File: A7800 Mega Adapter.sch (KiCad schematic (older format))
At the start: 8 parts, among them J1 Atari 7800, J2 Mega Drive, Q1 2N3906, Q2 2N3906

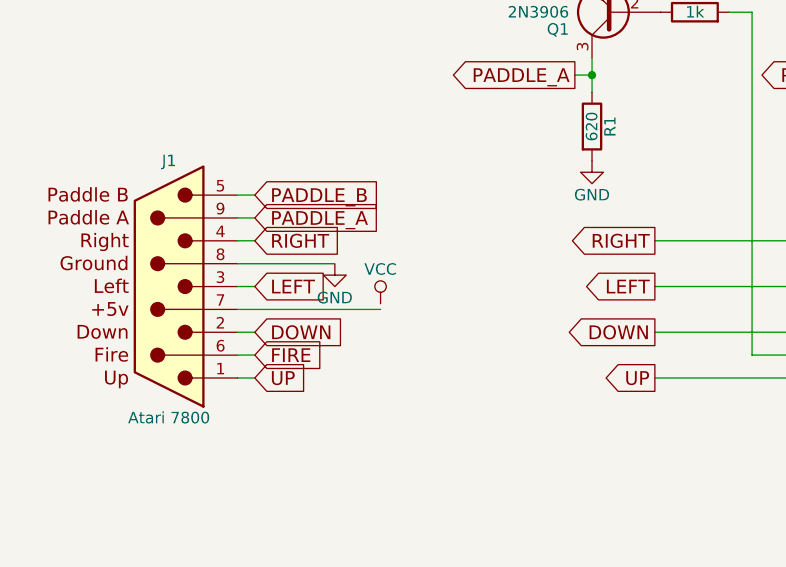
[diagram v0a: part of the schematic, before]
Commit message: Fixed VCC wire
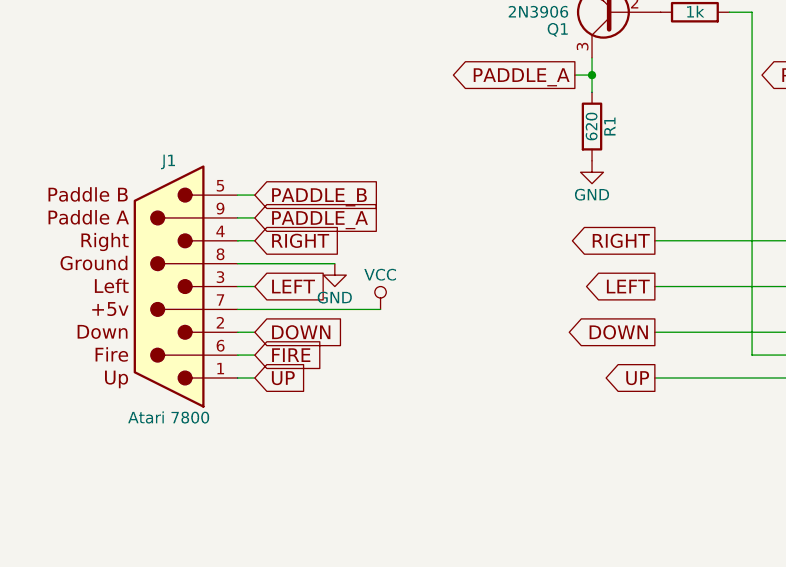
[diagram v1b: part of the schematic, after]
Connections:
- net VCC: now also J1.7 (VCC)
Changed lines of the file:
@@
 LIBS:sega_joypad
 LIBS:74hct4053
-LIBS:A7800 Mega Switcher-cache
+LIBS:A7800 Mega Adapter-cache
 EELAYER 25 0
 EELAYER END
@@
 L VCC #PWR06
 U 1 1 5DA626F8
-P 4625 3975
-F 0 "#PWR06" H 4625 3825 50  0001 C CNN
-F 1 "VCC" H 4625 4125 50  0000 C CNN
-F 2 "" H 4625 3975 50  0001 C CNN
-F 3 "" H 4625 3975 50  0001 C CNN
-	1    4625 3975
-	1    0    0    -1
-$EndComp
+P 4625 4000
+F 0 "#PWR06" H 4625 3850 50  0001 C CNN
+F 1 "VCC" H 4625 4150 50  0000 C CNN
+F 2 "" H 4625 4000 50  0001 C CNN
+F 3 "" H 4625 4000 50  0001 C CNN
+	1    4625 4000
+	1    0    0    -1
+$EndComp
